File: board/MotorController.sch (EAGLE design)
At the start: 14 parts, among them IC1 7805T, U1 ATTINY84-20PU

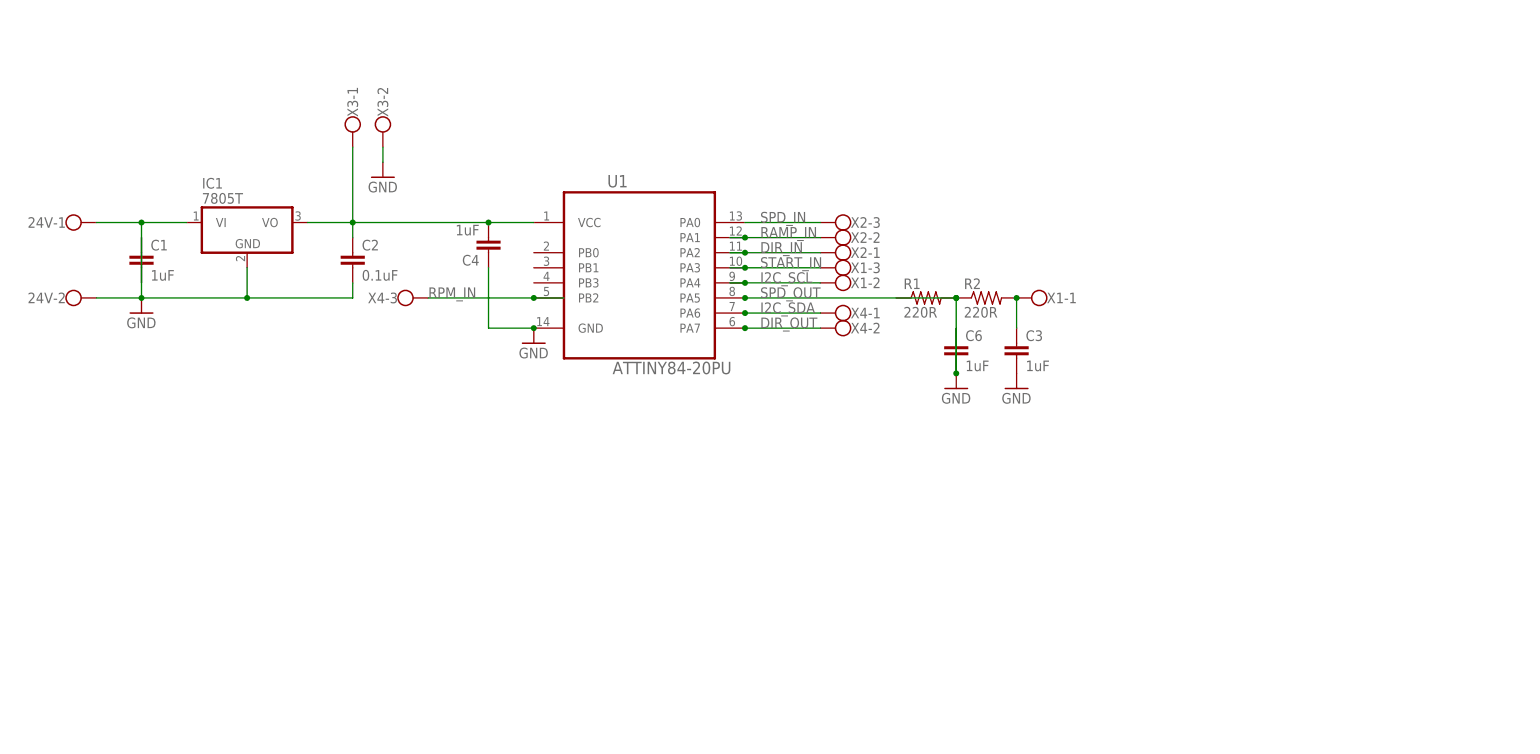
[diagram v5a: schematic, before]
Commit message: Initial pass at a PCB and added clock code
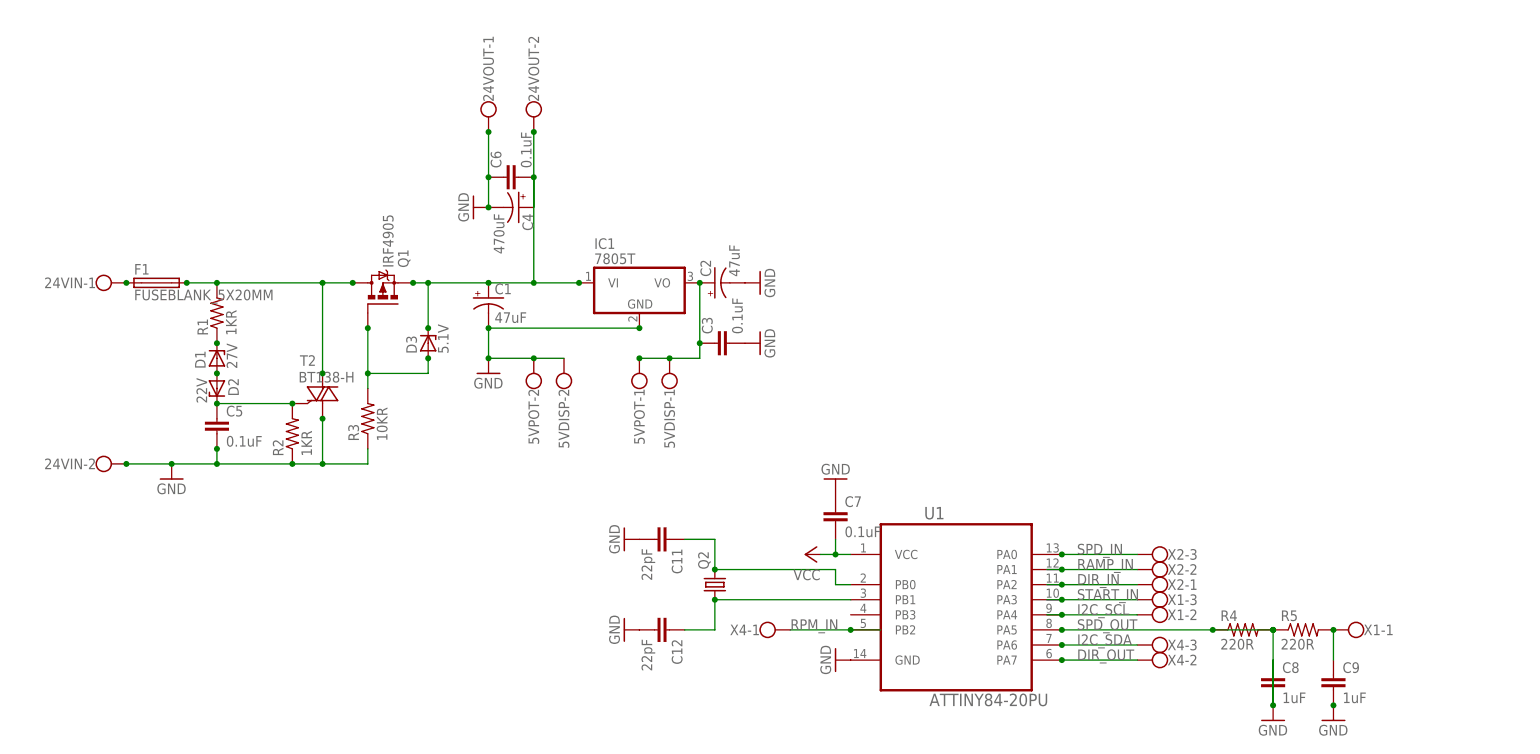
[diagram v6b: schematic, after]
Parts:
- removed 24V, X3: (no value), con-wago-500:W237-102
- added 24VIN, 24VOUT, 5VDISP, 5VPOT: (no value), con-wago-500:W237-102
- added C11, C12: 22pF, SparkFun-Capacitors:CAPPTH1
- added C5, C7: 0.1uF, SparkFun-Capacitors:CAPPTH1
- added C8, C9: 1uF, SparkFun-Capacitors:CAPPTH1
- added D1: 27V, diode:ZENER-DIODEZD-7.5
- added D2: 22V, diode:ZENER-DIODEZD-7.5
- added D3: 5.1V, diode:ZENER-DIODEZD-7.5
- added F1: FUSEBLANK_5X20MM, fuse:FUSEBLANK_5X20MM
- added Q1: IRF4905, transistor-power:IRF4905
- added Q2: (no value), crystal:CRYSTALHC18U-V
- added R3: 10KR, SparkFun-Resistors:RESISTORAXIAL-0.3
- added R4, R5: 220R, SparkFun-Resistors:RESISTORAXIAL-0.3
- added T2: BT138-H, triac:BT138-H
- C1: value 1uF -> 47uF; device SparkFun-Capacitors:CAPPTH1 -> adafruit:CPOL-USE2.5-5
- C2: value 0.1uF -> 47uF; device SparkFun-Capacitors:CAPPTH1 -> adafruit:CPOL-USE2.5-5
- C3, C6: value 1uF -> 0.1uF
- C4: value 1uF -> 470uF; device SparkFun-Capacitors:CAPPTH1 -> adafruit:CPOL-USE2.5-5
- IC1: device linear:7805T -> adafruit:7805T
- R1, R2: value 220R -> 1KR
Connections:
- removed net +24V: 24V-1.KL, C1.2, IC1.VI
- removed net N$1: C6.2, R1.1, R2.1
- removed net N$2: C3.1, R2.2, X1-1.KL
- removed net VCC: C2.1, C4.2, IC1.VO, U1.VCC, X3-1.KL
- new net 24V: F1.2, Q1.D, R1.2, T2.A2
- new net 24V-PROTECTED: 24VOUT-2.KL, C1.+, C4.+, C6.2, D3.C, IC1.VI, Q1.S
- new net 5V: 5VDISP-1.KL, 5VPOT-1.KL, C2.+, C3.1, C7.2, IC1.VO, U1.VCC
- new net N$10: C9.1, R5.2, X1-1.KL
- new net N$12: C12.1, Q2.1, U1.PB1
- new net N$13: C11.1, Q2.2, U1.PB0
- new net N$3: 24VIN-1.KL, F1.1
- new net N$4: D3.A, Q1.G, R3.2
- new net N$5: D1.C, R1.1
- new net N$6: D1.A, D2.A
- new net N$7: C5.1, D2.C, R2.2, T2.G
- new net N$8: C8.2, R4.1, R5.1
- net GND: now also 24VIN-2.KL, 24VOUT-1.KL, 5VDISP-2.KL, 5VPOT-2.KL, C1.-, C11.2, C12.2, C2.-, C4.-, C5.2, C7.1, C8.1, C9.2, R2.1, R3.1, T2.A1; no longer 24V-2.KL, C1.1, C2.2, C4.1, X3-2.KL
- net I2C_SDA: now also X4-3.KL; no longer X4-1.KL
- net RPM_IN: now also X4-1.KL; no longer X4-3.KL
- net SPD_OUT: now also R4.2; no longer R1.2
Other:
- moved on the sheet: C3, C6, IC1, R1, R2, U1, X1-1, X1-2, X1-3, X2-1, X2-2, X2-3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

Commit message: PCB improvements
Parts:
- removed IC1: 7805T, adafruit:7805T
- removed T2: BT138-H, triac:BT138-H
- removed X1, X2, X4: (no value), con-wago-500:W237-103
- added DC1: OKI-78SR-5/1.5-W36H-C, SaintGimp:DC-CONV
- added IO1, IO2, IO3: (no value), SaintGimp:SCREW-TERM-3
- added R6, R7: 2.2K, SaintGimp:RESISTOR-7.5MM
- added T1: BT139X-600E, SaintGimp:TRIAC-H
- 24VIN, 24VOUT, 5VDISP, 5VPOT: device con-wago-500:W237-102 -> SaintGimp:SCREW-TERM-2
- C11, C12, C3, C5, C6, C7, C8, C9: device SparkFun-Capacitors:CAPPTH1 -> SaintGimp:CAPACITOR-5MM
- C4: device adafruit:CPOL-USE2.5-5 -> SaintGimp:CAP-POL-25-14
- D1, D2, D3: device diode:ZENER-DIODEZD-7.5 -> SaintGimp:ZENER-7.5
- Q1: value IRF4905 -> IPP80P03P4L-04; device transistor-power:IRF4905 -> SaintGimp:P-MOSFET-H
- Q2: value (none) -> 8Mhz; device crystal:CRYSTALHC18U-V -> SaintGimp:CRYSTAL-V
- R1, R2: value 1KR -> 1K; device SparkFun-Resistors:RESISTORAXIAL-0.3 -> SaintGimp:RESISTOR-7.5MM
- R3: value 10KR -> 10K; device SparkFun-Resistors:RESISTORAXIAL-0.3 -> SaintGimp:RESISTOR-7.5MM
- R4, R5: value 220R -> 220; device SparkFun-Resistors:RESISTORAXIAL-0.3 -> SaintGimp:RESISTOR-7.5MM
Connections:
- removed net N$8: C8.2, R4.1, R5.1
- new net N$1: C8.1, R4.1, R5.1
- net 24V: now also T1.A2; no longer T2.A2
- net 24V-PROTECTED: now also 24VOUTT2.KL, DC1.IN; no longer 24VOUT-2.KL, IC1.VI
- net 5V: now also 5VDISPT1.KL, 5VPOTT1.KL, DC1.OUT, R6.2, R7.1; no longer 5VDISP-1.KL, 5VPOT-1.KL, IC1.VO
- net DIR_IN: now also IO3T1.KL; no longer X2-1.KL
- net DIR_OUT: now also IO1T2.KL; no longer X4-2.KL
- net GND: now also 24VINT2.KL, 24VOUTT1.KL, 5VDISPT2.KL, 5VPOTT2.KL, C8.2, DC1.GND, T1.A1; no longer 24VIN-2.KL, 24VOUT-1.KL, 5VDISP-2.KL, 5VPOT-2.KL, C8.1, IC1.GND, T2.A1
- net I2C_SCL: now also IO2T2.KL, R6.1; no longer X1-2.KL
- net I2C_SDA: now also IO1T3.KL, R7.2; no longer X4-3.KL
- net N$10: now also IO2T1.KL; no longer X1-1.KL
- net N$3: now also 24VINT1.KL; no longer 24VIN-1.KL
- net N$7: now also T1.G; no longer T2.G
- net RAMP_IN: now also IO3T2.KL; no longer X2-2.KL
- net RPM_IN: now also IO1T1.KL; no longer X4-1.KL
- net SPD_IN: now also IO3T3.KL; no longer X2-3.KL
- net START_IN: now also IO2T3.KL; no longer X1-3.KL
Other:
- moved on the sheet: C2, C3, C8, C9, R4, R5

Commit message: Update with current design rules and current library
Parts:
- 24VIN, 24VOUT, 5VDISP, 5VPOT: value (none) -> SCREW-TERM-2
- C1, C2: device adafruit:CPOL-USE2.5-5 -> SaintGimp:CAP-POL-2.5-5
- F1: device fuse:FUSEBLANK_5X20MM -> SaintGimp:FUSE
- IO1, IO2, IO3: value (none) -> SCREW-TERM-3
- Q1: device SaintGimp:P-MOSFET-H -> SaintGimp:IPP80P03P4L-04-H
- U1: device Atmel_By_element14_Batch_1:ATTINY84-20PU -> SaintGimp:ATTINY84-20PU
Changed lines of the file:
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@@
 <?xml version="1.0" encoding="utf-8"?>
 <!DOCTYPE eagle SYSTEM "eagle.dtd">
-<eagle version="6.5.0">
+<eagle version="7.2.0">
 <drawing>
 <settings>
@@
 <layer number="56" name="wert" color="7" fill="1" visible="no" active="no"/>
 <layer number="57" name="tCAD" color="7" fill="1" visible="no" active="no"/>
+<layer number="90" name="Modules" color="5" fill="1" visible="yes" active="yes"/>
 <layer number="91" name="Nets" color="2" fill="1" visible="yes" active="yes"/>
 <layer number="92" name="Busses" color="1" fill="1" visible="yes" active="yes"/>
@@
 <layer number="97" name="Info" color="7" fill="1" visible="yes" active="yes"/>
 <layer number="98" name="Guide" color="6" fill="1" visible="yes" active="yes"/>
+<layer number="99" name="SpiceOrder" color="7" fill="1" visible="yes" active="yes"/>
 <layer number="100" name="Muster" color="7" fill="1" visible="no" active="no"/>
 <layer number="101" name="Patch_Top" color="12" fill="4" visible="yes" active="yes"/>
@@
 <layer number="111" name="LPC17xx" color="7" fill="1" visible="yes" active="yes"/>
 <layer number="112" name="tSilk" color="7" fill="1" visible="yes" active="yes"/>
+<layer number="113" name="IDFDebug" color="7" fill="1" visible="yes" active="yes"/>
 <layer number="116" name="Patch_BOT" color="9" fill="4" visible="yes" active="yes"/>
 <layer number="121" name="_tsilk" color="7" fill="1" visible="yes" active="yes"/>
@@
 <layer number="223" name="223bmp" color="24" fill="1" visible="no" active="no"/>
 <layer number="224" name="224bmp" color="25" fill="1" visible="no" active="no"/>
+<layer number="225" name="225bmp" color="7" fill="1" visible="yes" active="yes"/>
+<layer number="226" name="226bmp" color="7" fill="1" visible="yes" active="yes"/>
+<layer number="227" name="227bmp" color="7" fill="1" visible="yes" active="yes"/>
+<layer number="228" name="228bmp" color="7" fill="1" visible="yes" active="yes"/>
+<layer number="229" name="229bmp" color="7" fill="1" visible="yes" active="yes"/>
+<layer number="230" name="230bmp" color="7" fill="1" visible="yes" active="yes"/>
+<layer number="231" name="231bmp" color="7" fill="1" visible="yes" active="yes"/>
 <layer number="248" name="Housing" color="7" fill="1" visible="yes" active="yes"/>
 <layer number="249" name="Edge" color="7" fill="1" visible="yes" active="yes"/>
@@
 <layer number="251" name="SMDround" color="12" fill="11" visible="no" active="no"/>
 <layer number="254" name="cooling" color="7" fill="1" visible="yes" active="yes"/>
+<layer number="255" name="routoute" color="7" fill="1" visible="yes" active="yes"/>
 </layers>
 <schematic xreflabel="%F%N/%S.%C%R" xrefpart="/%S.%C%R">
@@
 <parts>
 <part name="24VIN" library="SaintGimp" deviceset="SCREW-TERM-2" device=""/>
-<part name="GND1" library="supply1" deviceset="GND" device=""/>
-<part name="GND4" library="supply1" deviceset="GND" device=""/>
-<part name="GND5" library="supply1" deviceset="GND" device=""/>
+<part name="GND1" library="SaintGimp" deviceset="GND" device=""/>
+<part name="GND4" library="SaintGimp" deviceset="GND" device=""/>
+<part name="GND5" library="SaintGimp" deviceset="GND" device=""/>
 <part name="24VOUT" library="SaintGimp" deviceset="SCREW-TERM-2" device=""/>
 <part name="5VPOT" library="SaintGimp" deviceset="SCREW-TERM-2" device=""/>
 <part name="5VDISP" library="SaintGimp" deviceset="SCREW-TERM-2" device=""/>
-<part name="C1" library="adafruit" deviceset="CPOL-US" device="E2.5-5" value="47uF"/>
+<part name="C1" library="SaintGimp" deviceset="CAP-POL" device="-2.5-5" value="47uF"/>
 <part name="C4" library="SaintGimp" deviceset="CAP-POL" device="-25-14" value="470uF"/>
-<part name="F1" library="fuse" deviceset="FUSE" device="BLANK_5X20MM" value="FUSEBLANK_5X20MM"/>
+<part name="F1" library="SaintGimp" deviceset="FUSE" device="" value="FUSEBLANK_5X20MM"/>
 <part name="T1" library="SaintGimp" deviceset="TRIAC" device="-H" value="BT139X-600E"/>
 <part name="D2" library="SaintGimp" deviceset="ZENER" device="-7.5" value="22V"/>
@@
 <part name="C5" library="SaintGimp" deviceset="CAPACITOR-*" device="5MM" value="0.1uF"/>
 <part name="R2" library="SaintGimp" deviceset="RESISTOR-*" device="7.5MM" value="1K"/>
-<part name="Q1" library="SaintGimp" deviceset="P-MOSFET" device="-H" value="IPP80P03P4L-04"/>
+<part name="Q1" library="SaintGimp" deviceset="IPP80P03P4L-04" device="-H" value="IPP80P03P4L-04"/>
 <part name="R3" library="SaintGimp" deviceset="RESISTOR-*" device="7.5MM" value="10K"/>
 <part name="D3" library="SaintGimp" deviceset="ZENER" device="-7.5" value="5.1V"/>
-<part name="C2" library="adafruit" deviceset="CPOL-US" device="E2.5-5" value="47uF"/>
-<part name="GND2" library="supply1" deviceset="GND" device=""/>
+<part name="C2" library="SaintGimp" deviceset="CAP-POL" device="-2.5-5" value="47uF"/>
+<part name="GND2" library="SaintGimp" deviceset="GND" device=""/>
 <part name="C3" library="SaintGimp" deviceset="CAPACITOR-*" device="5MM" value="0.1uF"/>
-<part name="GND3" library="supply1" deviceset="GND" device=""/>
+<part name="GND3" library="SaintGimp" deviceset="GND" device=""/>
 <part name="C6" library="SaintGimp" deviceset="CAPACITOR-*" device="5MM" value="0.1uF"/>
-<part name="GND6" library="supply1" deviceset="GND" device=""/>
-<part name="U1" library="Atmel_By_element14_Batch_1" deviceset="ATTINY84-20PU" device=""/>
+<part name="GND6" library="SaintGimp" deviceset="GND" device=""/>
+<part name="U1" library="SaintGimp" deviceset="ATTINY84-20PU" device=""/>
 <part name="C7" library="SaintGimp" deviceset="CAPACITOR-*" device="5MM" value="0.1uF"/>
 <part name="R4" library="SaintGimp" deviceset="RESISTOR-*" device="7.5MM" value="220"/>
@@
 <part name="IO1" library="SaintGimp" deviceset="SCREW-TERM-3" device=""/>
 <part name="C8" library="SaintGimp" deviceset="CAPACITOR-*" device="5MM" value="1uF"/>
-<part name="GND7" library="supply1" deviceset="GND" device=""/>
+<part name="GND7" library="SaintGimp" deviceset="GND" device=""/>
 <part name="C9" library="SaintGimp" deviceset="CAPACITOR-*" device="5MM" value="1uF"/>
-<part name="GND8" library="supply1" deviceset="GND" device=""/>
+<part name="GND8" library="SaintGimp" deviceset="GND" device=""/>
 <part name="Q2" library="SaintGimp" deviceset="CRYSTAL" device="-V" value="8Mhz"/>
-<part name="GND10" library="supply1" deviceset="GND" device=""/>
+<part name="GND10" library="SaintGimp" deviceset="GND" device=""/>
 <part name="C11" library="SaintGimp" deviceset="CAPACITOR-*" device="5MM" value="22pF"/>
 <part name="C12" library="SaintGimp" deviceset="CAPACITOR-*" device="5MM" value="22pF"/>
-<part name="GND11" library="supply1" deviceset="GND" device=""/>
-<part name="GND12" library="supply1" deviceset="GND" device=""/>
-<part name="5V" library="supply1" deviceset="VCC" device="" value="5V"/>
-<part name="P+1" library="supply1" deviceset="VCC" device="" value="5V"/>
+<part name="GND11" library="SaintGimp" deviceset="GND" device=""/>
+<part name="GND12" library="SaintGimp" deviceset="GND" device=""/>
+<part name="5V" library="SaintGimp" deviceset="VCC" device="" value="5V"/>
+<part name="P+1" library="SaintGimp" deviceset="VCC" device="" value="5V"/>
 <part name="DC1" library="SaintGimp" deviceset="DC-CONV" device="" value="OKI-78SR-5/1.5-W36H-C"/>
 <part name="R6" library="SaintGimp" deviceset="RESISTOR-*" device="7.5MM" value="2.2K"/>
 <part name="R7" library="SaintGimp" deviceset="RESISTOR-*" device="7.5MM" value="2.2K"/>
-<part name="5V1" library="supply1" deviceset="VCC" device="" value="5V"/>
-<part name="5V2" library="supply1" deviceset="VCC" device="" value="5V"/>
+<part name="5V1" library="SaintGimp" deviceset="VCC" device="" value="5V"/>
+<part name="5V2" library="SaintGimp" deviceset="VCC" device="" value="5V"/>
 </parts>
 <sheets>
